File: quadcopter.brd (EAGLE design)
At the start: 134.1 x 134 mm, 81 parts, among them J1 ISP, U2 ATMEGA128RFA1

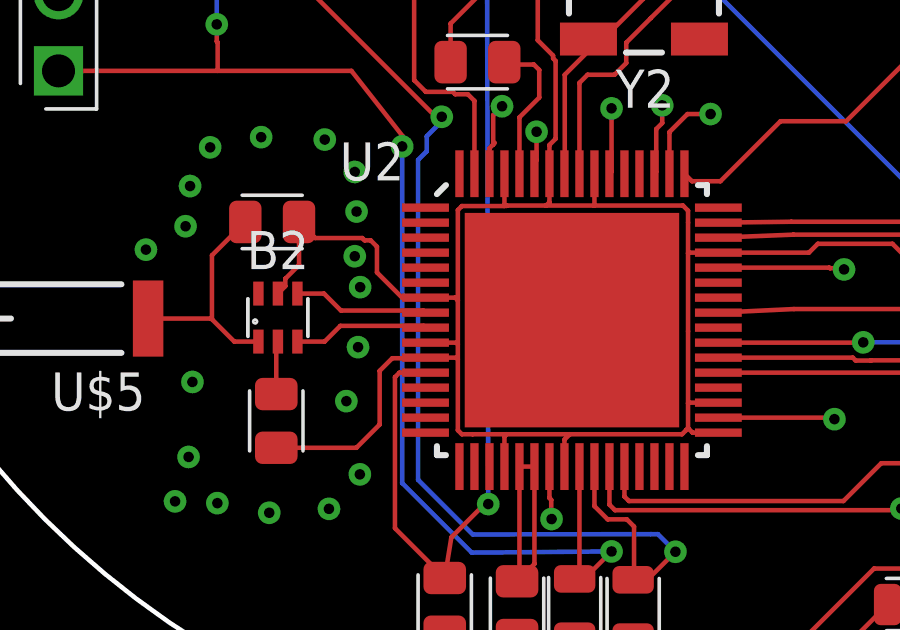
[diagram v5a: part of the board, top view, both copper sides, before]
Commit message: After fixing professor's comments V2
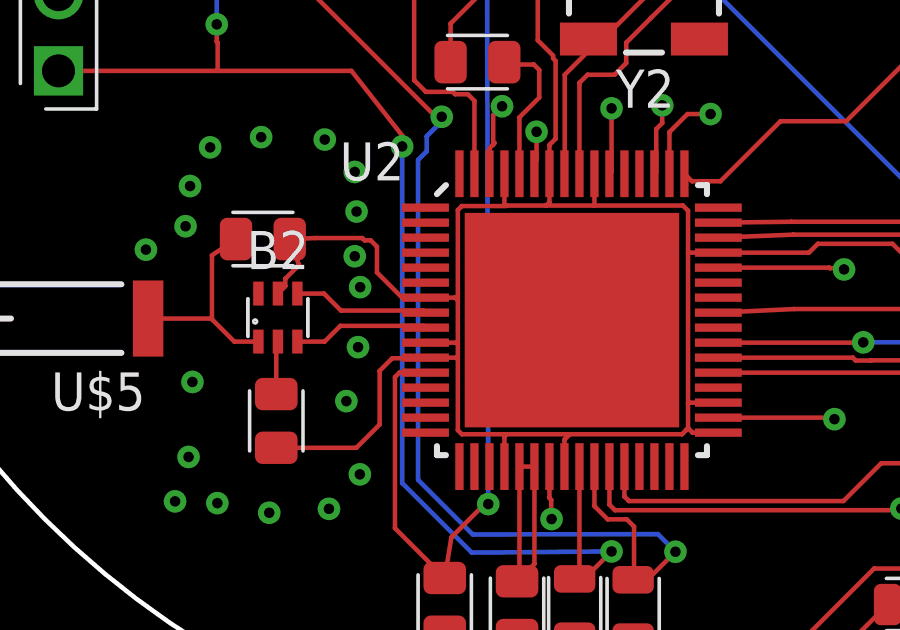
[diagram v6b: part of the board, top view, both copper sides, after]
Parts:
- moved C9 0.65 mm to (-21.8, -19.8)
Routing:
- net RFANT: track 7.70 -> 7.09 mm
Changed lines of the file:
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@@
 <attribute name="MPN" value="GRM21BR61E106KA73L" x="15.45" y="32.24" size="1.778" layer="27" rot="R270" display="off"/>
 </element>
-<element name="C9" library="quadparts_prebuilt" package="CAPC2012X140_HS" value="0.75pF" x="-21.472428125" y="-19.247015625">
-<attribute name="DIST" value="Digikey" x="-21.472428125" y="-19.247015625" size="1.778" layer="27" display="off"/>
-<attribute name="DISTPN" value="490-3585-1-ND" x="-21.472428125" y="-19.247015625" size="1.778" layer="27" display="off"/>
-<attribute name="MFR" value="Murata Electronics North America" x="-21.472428125" y="-19.247015625" size="1.778" layer="27" display="off"/>
-<attribute name="MPN" value="GQM2195C2AR75CB01D" x="-21.472428125" y="-19.247015625" size="1.778" layer="27" display="off"/>
+<element name="C9" library="quadparts_prebuilt" package="CAPC2012X140_HS" value="0.75pF" x="-21.782428125" y="-19.817015625">
+<attribute name="DIST" value="Digikey" x="-21.782428125" y="-19.817015625" size="1.778" layer="27" display="off"/>
+<attribute name="DISTPN" value="490-3585-1-ND" x="-21.782428125" y="-19.817015625" size="1.778" layer="27" display="off"/>
+<attribute name="MFR" value="Murata Electronics North America" x="-21.782428125" y="-19.817015625" size="1.778" layer="27" display="off"/>
+<attribute name="MPN" value="GQM2195C2AR75CB01D" x="-21.782428125" y="-19.817015625" size="1.778" layer="27" display="off"/>
 </element>
 <element name="D5" library="quadparts_prebuilt" package="LEDSC125X200X120-2_HS" value="green" x="-9.3" y="34.7">
@@
 <wire x1="-18.19" y1="-19.86" x2="-18.39185" y2="-19.86" width="0.1524" layer="1"/>
 <wire x1="-18.39185" y1="-19.86" x2="-18.46865" y2="-19.7832" width="0.1524" layer="1"/>
-<wire x1="-20.04124375" y1="-19.7832" x2="-20.577428125" y2="-19.247015625" width="0.1524" layer="1"/>
+<wire x1="-20.04124375" y1="-19.7832" x2="-20.887428125" y2="-19.817015625" width="0.1524" layer="1"/>
 <wire x1="-18.46865" y1="-19.7832" x2="-20.04124375" y2="-19.7832" width="0.1524" layer="1"/>
 <wire x1="-21.034725" y1="-21.13993125" x2="-21.034725" y2="-21.38821875" width="0.1524" layer="1"/>
 <wire x1="-21.034725" y1="-21.38821875" x2="-21.281125" y2="-21.63461875" width="0.1524" layer="1"/>
-<wire x1="-20.577428125" y1="-19.247015625" x2="-20.577428125" y2="-20.682634375" width="0.1524" layer="1"/>
+<wire x1="-20.887428125" y1="-19.817015625" x2="-20.577428125" y2="-20.682634375" width="0.1524" layer="1"/>
 <wire x1="-20.577428125" y1="-20.682634375" x2="-21.034725" y2="-21.13993125" width="0.1524" layer="1"/>
 <wire x1="-21.3354375" y1="-26.774475" x2="-18.664475" y2="-26.774475" width="0.1524" layer="1"/>
@@
 <wire x1="-7.6764" y1="-26.1896875" x2="-7.6764" y2="-26.1864" width="0.1524" layer="1"/>
 <wire x1="-7.61" y1="-26.12" x2="-7.6764" y2="-26.1864" width="0.1524" layer="1"/>
-<wire x1="-7.61" y1="-25.29" x2="-7.61" y2="-22.89" width="0.1524" layer="1"/>
-<wire x1="-7.61" y1="-22.89" x2="-7.61" y2="-20.29" width="0.1524" layer="1"/>
+<wire x1="-7.61" y1="-25.29" x2="-7.61" y2="-20.29" width="0.1524" layer="1"/>
 <wire x1="-7.61" y1="-25.29" x2="-7.61" y2="-26.12" width="0.1524" layer="1"/>
-<wire x1="-7.61" y1="-20.29" x2="-7.61" y2="-19.27" width="0.1524" layer="1"/>
-<wire x1="-7.61" y1="-19.27" x2="-7.61" y2="-18.87" width="0.1524" layer="1"/>
+<wire x1="-7.61" y1="-20.29" x2="-7.61" y2="-18.87" width="0.1524" layer="1"/>
 <wire x1="-7.61" y1="-18.87" x2="-7.78" y2="-18.7" width="0.1524" layer="1"/>
 <wire x1="-10.74" y1="-18.7" x2="-12.34" y2="-18.7" width="0.1524" layer="1"/>
@@
 <wire x1="-15.2836" y1="-23.82" x2="-15.2836" y2="-26.1896875" width="0.1524" layer="1"/>
 <wire x1="-13.67" y1="-26.3236" x2="-11.55" y2="-26.3236" width="0.1524" layer="1"/>
-<wire x1="-13.67" y1="-26.3236" x2="-14.79" y2="-26.3236" width="0.1524" layer="1"/>
-<wire x1="-14.79" y1="-26.3236" x2="-15.1496875" y2="-26.3236" width="0.1524" layer="1"/>
+<wire x1="-13.67" y1="-26.3236" x2="-15.1496875" y2="-26.3236" width="0.1524" layer="1"/>
 <wire x1="-11.55" y1="-26.3236" x2="-7.8103125" y2="-26.3236" width="0.1524" layer="1"/>
 <wire x1="-12.23" y1="-18.59" x2="-12.23" y2="-17.639" width="0.1524" layer="1"/>
@@
 <wire x1="-23.48" y1="-22.49" x2="-23.503103125" y2="-22.466896875" width="0.1524" layer="1"/>
 <wire x1="-23.48" y1="-22.49" x2="-23.48" y2="-20.3595875" width="0.1524" layer="1"/>
-<wire x1="-23.48" y1="-20.3595875" x2="-22.367428125" y2="-19.247015625" width="0.1524" layer="1"/>
+<wire x1="-23.48" y1="-20.3595875" x2="-22.677428125" y2="-19.817015625" width="0.1524" layer="1"/>
 <wire x1="-21.931125" y1="-23.23461875" x2="-22.73538125" y2="-23.23461875" width="0.1524" layer="1"/>
 <wire x1="-22.73538125" y1="-23.23461875" x2="-23.48" y2="-22.49" width="0.1524" layer="1"/>

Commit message: After fixing professor's comments V3
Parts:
- moved C19 35.4 mm to (7.40, 1.44), turned to 270 degrees
- moved C17 24.3 mm to (4.45, 2.46), turned to 180 degrees
- moved C1 4.41 mm to (-9.24, -11.2)
- moved C2 3.42 mm to (-12.6, -11.2)
- moved Y2 3.03 mm to (-11.2, -14.1)
- moved C11 1.36 mm to (-15.6, -12.9), turned to 90 degrees
- moved C21 1.08 mm to (-1.91, -4.71)
- moved C20 1.03 mm to (0.36, -4.69)
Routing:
- net PWM4: track 106.5 -> 72.4 mm, vias 3 -> 1
- net GND: track 231.5 -> 205.3 mm
- net VBAT: track 237.7 -> 216.9 mm
- net 3V: track 198.6 -> 185.2 mm, vias 21 -> 20
- net PWM2: track 110.9 -> 119.2 mm
- net PWM3: track 99.9 -> 94.1 mm, vias 6 -> 3
- net SDA: track 89.1 -> 94.1 mm
- net PWM1: track 71.0 -> 74.7 mm
- net N$4: track 11.9 -> 8.35 mm
- net N$3: track 11.3 -> 7.85 mm
- net SCL: track 94.1 -> 96.8 mm
- net N$33: track 2.96 -> 1.89 mm
- net N$23: track 2.66 -> 1.63 mm
- net BAT_GND: track 307.1 -> 306.2 mm
- net AVDD: track 5.25 -> 5.86 mm

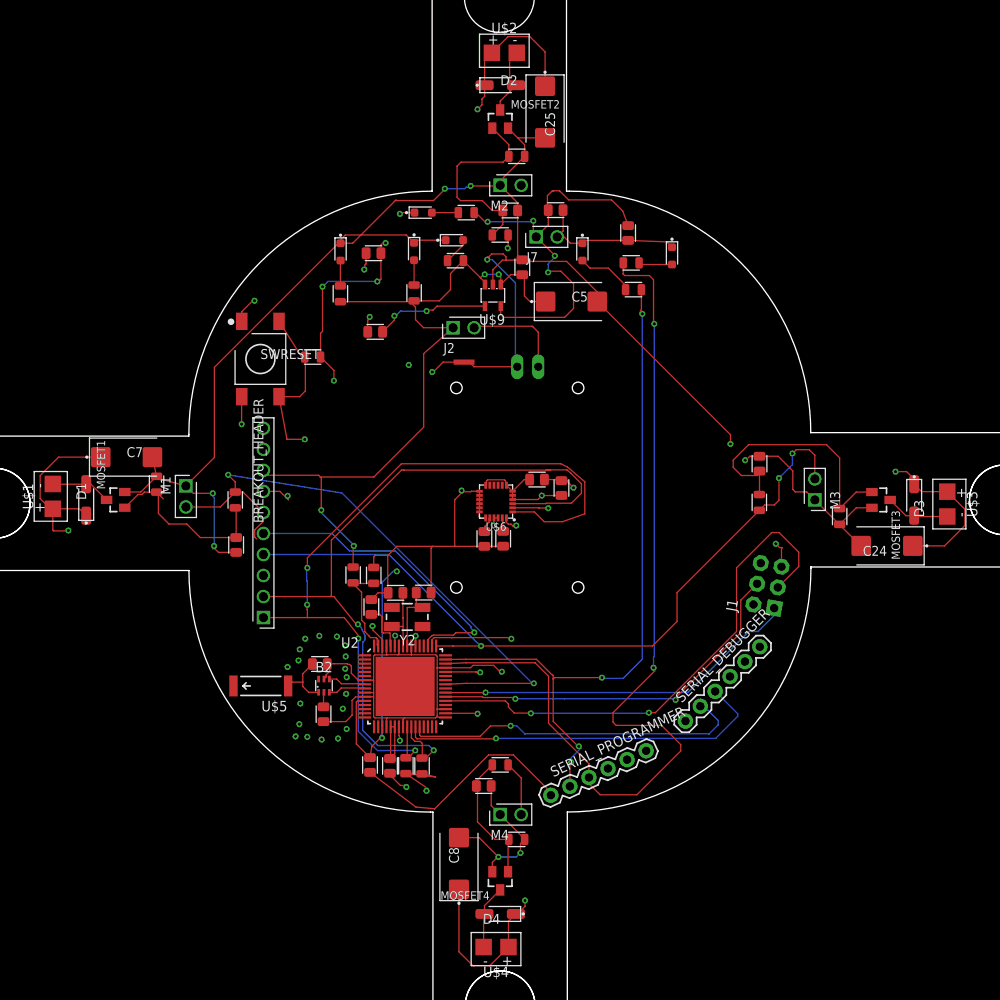
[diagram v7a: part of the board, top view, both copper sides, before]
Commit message: After fixing professor's comments V3 (Fixed wires)
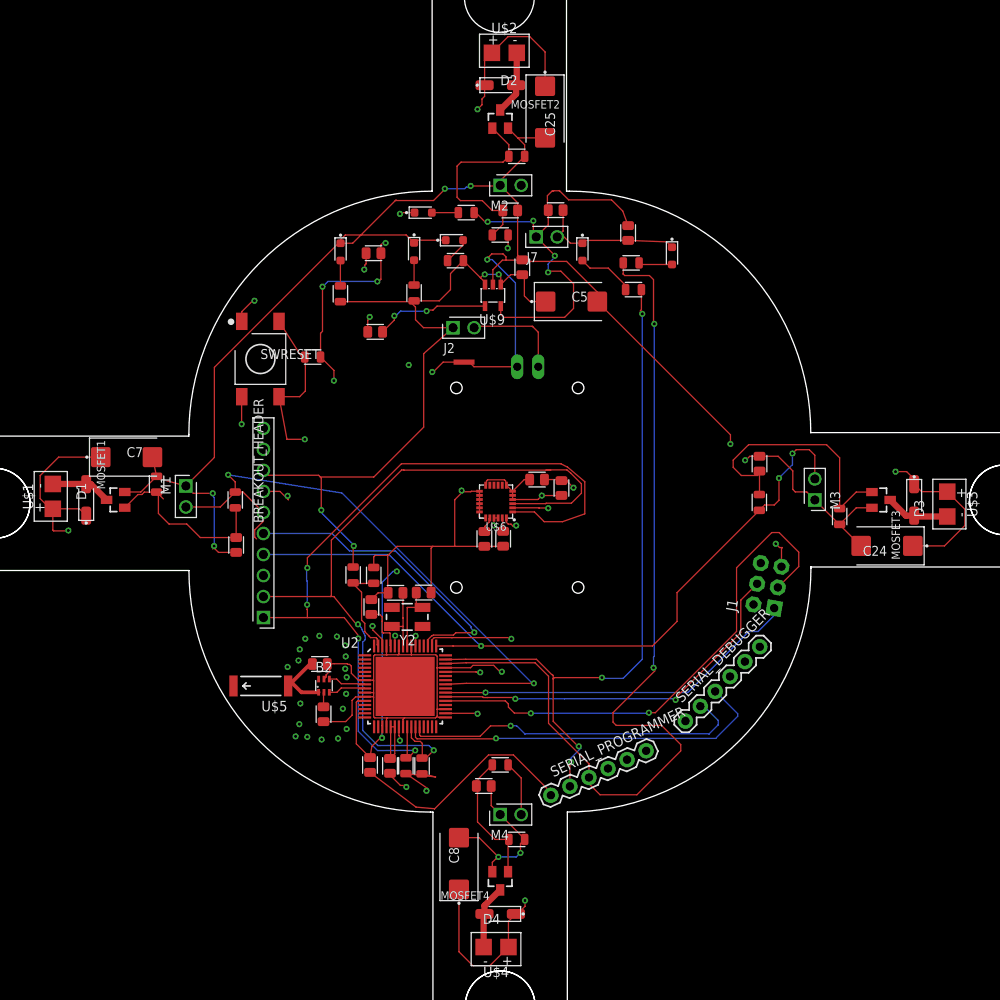
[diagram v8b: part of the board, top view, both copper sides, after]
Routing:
- net RFANT: track 7.36 -> 8.06 mm
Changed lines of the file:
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@@
 <setting verticaltext="up"/>
 </settings>
-<grid distance="0.01" unitdist="mm" unit="mm" style="lines" multiple="1" display="no" altdistance="0.1" altunitdist="mil" altunit="mm"/>
+<grid distance="0.393700787" unitdist="mil" unit="mil" style="lines" multiple="1" display="no" altdistance="0.1" altunitdist="mil" altunit="mm"/>
 <layers>
 <layer number="1" name="Top" color="4" fill="1" visible="yes" active="yes"/>
@@
 <contactref element="C9" pad="1"/>
 <contactref element="U$5" pad="FEED"/>
-<wire x1="-21.931125" y1="-23.23461875" x2="-23.13538125" y2="-23.23461875" width="0.1524" layer="1"/>
-<wire x1="-23.13538125" y1="-23.23461875" x2="-23.84" y2="-22.53" width="0.1524" layer="1"/>
-<wire x1="-23.84" y1="-20.9795875" x2="-22.677428125" y2="-19.817015625" width="0.1524" layer="1"/>
-<wire x1="-23.84" y1="-22.53" x2="-23.84" y2="-22" width="0.1524" layer="1"/>
-<wire x1="-23.84" y1="-22" x2="-23.84" y2="-20.9795875" width="0.1524" layer="1"/>
-<wire x1="-23.84" y1="-22" x2="-25.140771875" y2="-22" width="0.1524" layer="1"/>
-<wire x1="-25.140771875" y1="-22" x2="-25.60766875" y2="-22.466896875" width="0.1524" layer="1"/>
+<wire x1="-22.9577875" y1="-19.817015625" x2="-22.677428125" y2="-19.817015625" width="0.4572" layer="1"/>
+<wire x1="-22.677428125" y1="-19.817015625" x2="-22.9577875" y2="-19.817015625" width="0.4572" layer="1"/>
+<wire x1="-25.1903875" y1="-22.049615625" x2="-22.9577875" y2="-19.817015625" width="0.4572" layer="1"/>
+<wire x1="-25.1903875" y1="-22.049615625" x2="-25.60766875" y2="-22.466896875" width="0.4572" layer="1"/>
+<wire x1="-21.931125" y1="-23.23461875" x2="-24.005384375" y2="-23.23461875" width="0.4572" layer="1"/>
+<wire x1="-24.005384375" y1="-23.23461875" x2="-25.1903875" y2="-22.049615625" width="0.4572" layer="1"/>
 </signal>
 <signal name="RESET">
@@
 <contactref element="MOSFET1" pad="3"/>
 <contactref element="D1" pad="A"/>
-<wire x1="-49.43" y1="1.9" x2="-50" y2="1.9" width="0.1524" layer="1"/>
-<wire x1="-49.43" y1="1.9" x2="-47.54" y2="0.01" width="0.1524" layer="1"/>
-<wire x1="-50" y1="1.9" x2="-54" y2="1.9" width="0.1524" layer="1"/>
-<wire x1="-54" y1="1.9" x2="-54.03" y2="1.93" width="0.1524" layer="1"/>
+<wire x1="-50.59" y1="1.9" x2="-50" y2="1.9" width="0.1524" layer="1"/>
+<wire x1="-54.03" y1="1.93" x2="-50.62" y2="1.93" width="0.762" layer="1"/>
+<wire x1="-50.62" y1="1.93" x2="-50.59" y2="1.9" width="0.762" layer="1"/>
+<wire x1="-50" y1="1.9" x2="-49.43" y2="1.9" width="0.762" layer="1"/>
+<wire x1="-49.43" y1="1.9" x2="-47.54" y2="0.01" width="0.762" layer="1"/>
 </signal>
 <signal name="PWM1">
@@
 <contactref element="MOSFET2" pad="3"/>
 <contactref element="D2" pad="A"/>
-<wire x1="0" y1="47.1" x2="0" y2="48.17" width="0.1524" layer="1"/>
-<wire x1="0" y1="48.17" x2="1.14" y2="49.31" width="0.1524" layer="1"/>
-<wire x1="1.14" y1="49.31" x2="1.92" y2="50.09" width="0.1524" layer="1"/>
-<wire x1="1.14" y1="49.31" x2="1.14" y2="53.14" width="0.1524" layer="1"/>
 <wire x1="1.14" y1="53.14" x2="2" y2="54" width="0.1524" layer="1"/>
+<wire x1="2" y1="54" x2="2" y2="50.17" width="0.762" layer="1"/>
+<wire x1="2" y1="50.17" x2="1.92" y2="50.09" width="0.762" layer="1"/>
+<wire x1="1.92" y1="50.09" x2="1.92" y2="49.02" width="0.762" layer="1"/>
+<wire x1="1.92" y1="49.02" x2="0" y2="47.1" width="0.762" layer="1"/>
 </signal>
 <signal name="PWM2">
@@
 <contactref element="MOSFET3" pad="3"/>
 <contactref element="D3" pad="A"/>
-<wire x1="54" y1="-2" x2="50.1" y2="-2" width="0.1524" layer="1"/>
 <wire x1="50.1" y1="-2" x2="50" y2="-1.9" width="0.1524" layer="1"/>
-<wire x1="50" y1="-1.9" x2="49" y2="-1.9" width="0.1524" layer="1"/>
-<wire x1="49" y1="-1.9" x2="47.1" y2="0" width="0.1524" layer="1"/>
+<wire x1="54" y1="-2" x2="50.1" y2="-2" width="0.762" layer="1"/>
+<wire x1="50.1" y1="-2" x2="50" y2="-1.9" width="0.762" layer="1"/>
+<wire x1="50" y1="-1.9" x2="49" y2="-1.9" width="0.762" layer="1"/>
+<wire x1="49" y1="-1.9" x2="47.1" y2="0" width="0.762" layer="1"/>
 </signal>
 <signal name="PWM3">
@@
 <contactref element="MOSFET4" pad="3"/>
 <contactref element="D4" pad="A"/>
-<wire x1="-2" y1="-54" x2="-2" y2="-50.1" width="0.1524" layer="1"/>
 <wire x1="-2" y1="-50.1" x2="-1.9" y2="-50" width="0.1524" layer="1"/>
-<wire x1="-1.9" y1="-50" x2="-1.9" y2="-49" width="0.1524" layer="1"/>
-<wire x1="-1.9" y1="-49" x2="0" y2="-47.1" width="0.1524" layer="1"/>
+<wire x1="-2" y1="-54" x2="-2" y2="-50.1" width="0.762" layer="1"/>
+<wire x1="-1.9" y1="-50" x2="-1.9" y2="-49" width="0.762" layer="1"/>
+<wire x1="-1.9" y1="-49" x2="0" y2="-47.1" width="0.762" layer="1"/>
 </signal>
 <signal name="PWM4">
